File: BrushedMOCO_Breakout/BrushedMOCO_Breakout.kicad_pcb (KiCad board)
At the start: 2 copper layers, 24 parts, among them Q1 Si4156DY, Q2 Si4156DY, Q3 Si4156DY, Q4 Si4156DY, U1 74LVC2G04, U2 IRS2308, U3 IRS2308

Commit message: obscenely rough draft
sorry, this one may hurt to look at
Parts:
- added REF**: 4_40_Hole, MRDT_Drill_Holes:4_40_Hole, F.Cu at (131.1, 75.7)
- added REF**: 4_40_Hole, MRDT_Drill_Holes:4_40_Hole, F.Cu at (174.0, 75.7)
- added REF**: 4_40_Hole, MRDT_Drill_Holes:4_40_Hole, F.Cu at (174.0, 39.4)
- added REF**: 4_40_Hole, MRDT_Drill_Holes:4_40_Hole, F.Cu at (131.1, 39.4)
- moved Q4 27.4 mm to (157.6, 68.6), turned to -90 degrees
- moved Q3 24.0 mm to (164.2, 63.7), turned to 90 degrees
- moved R6 22.0 mm to (161.8, 39.9), turned to 90 degrees
- moved D1 21.4 mm to (145.0, 39.9), turned to 90 degrees
- moved Q1 20.4 mm to (140.6, 63.9), turned to -90 degrees
- moved U2 17.7 mm to (140.6, 41.8), turned to -90 degrees
- moved Q2 17.6 mm to (140.6, 50.5), turned to -90 degrees
- moved C2 16.0 mm to (146.3, 57.4), turned to 0 degrees
- moved D4 14.3 mm to (161.8, 44.1), turned to -90 degrees
- moved R1 13.1 mm to (145.0, 44.1)
- moved R5 13.1 mm to (160.0, 58.3)
- moved R2 13.1 mm to (138.7, 58.2)
- moved R3 11.4 mm to (136.4, 46.2), turned to -90 degrees
- moved C4 9.04 mm to (168.4, 49.9)
- moved D3 8.80 mm to (166.1, 47.8), turned to -90 degrees
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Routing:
- net +12V: track 0.00 -> 80.8 mm, vias 0 -> 5
- net /M-: track 0.00 -> 51.4 mm, vias 0 -> 2
- net (no net): track 0.00 -> 39.4 mm, vias 0 -> 2
- net /M+: track 0.00 -> 37.8 mm
- net Net-(D2-K): track 0.00 -> 32.0 mm, vias 0 -> 2
- net PWM_FWD: track 0.00 -> 23.9 mm, vias 0 -> 2
- net PWM_RVS: track 0.00 -> 18.8 mm, vias 0 -> 2
- net Net-(D1-A): track 0.00 -> 18.5 mm
- net Net-(D3-K): track 0.00 -> 15.8 mm
- net Net-(D4-A): track 0.00 -> 13.4 mm
- net Net-(Q4-G): track 0.00 -> 9.94 mm
- net +3V3: track 0.00 -> 9.52 mm
- net Net-(Q3-G): track 0.00 -> 7.27 mm
- net Net-(U2-LO): track 0.00 -> 2.70 mm
- net Net-(Q2-G): track 0.00 -> 2.64 mm
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- added copper zone on B.Cu, net GND
- added copper zone on F.Cu, net GND
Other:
- board outline added: 51.1 x 44.5 mm

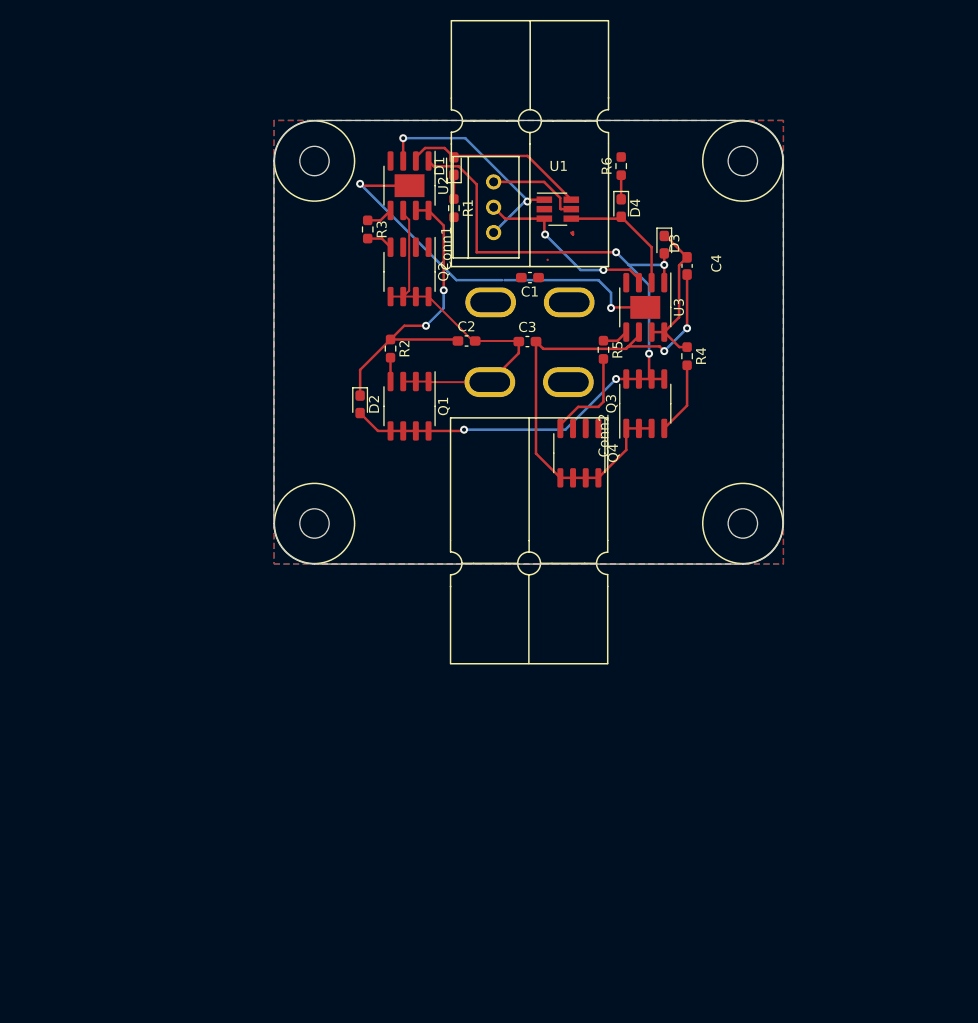
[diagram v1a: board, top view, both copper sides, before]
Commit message: A general outline of where stuff should go
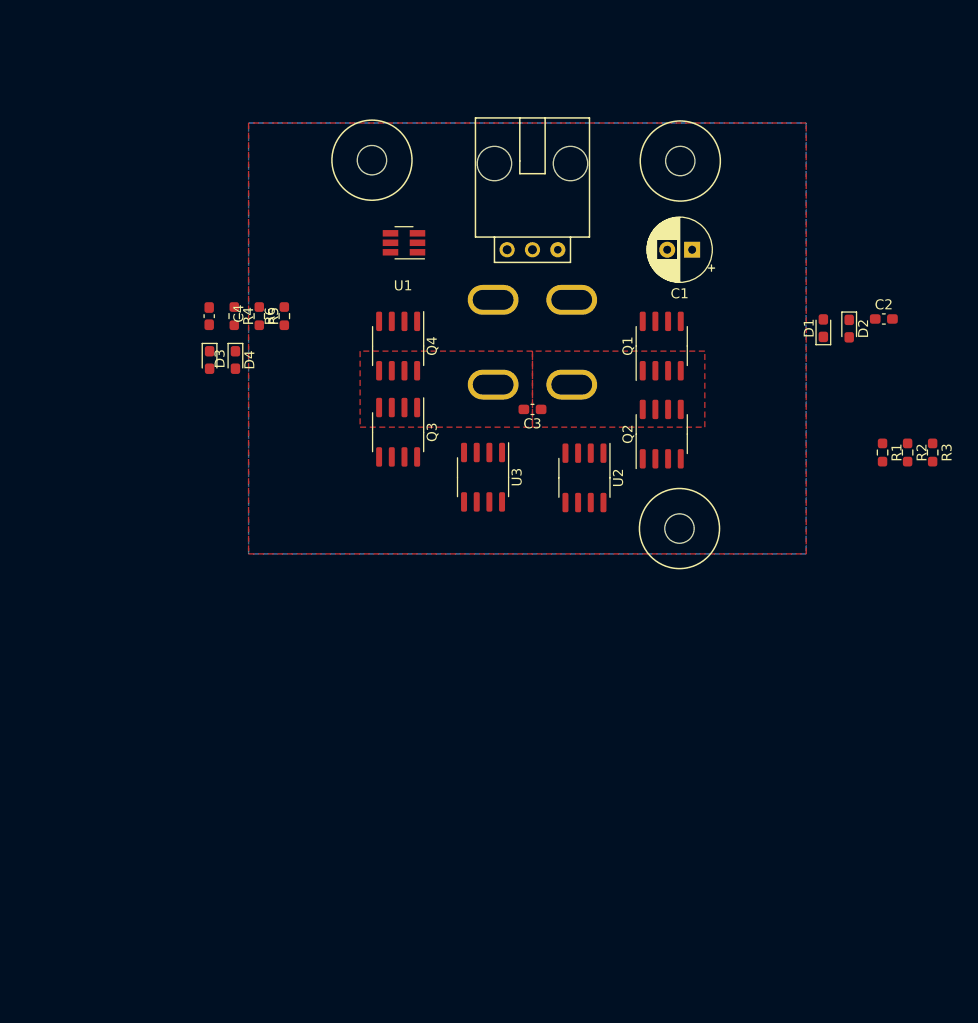
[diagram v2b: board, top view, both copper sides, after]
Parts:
- removed the REF** at (131.1, 75.7)
- removed the REF** at (174.0, 75.7)
- removed the REF** at (174.0, 39.4)
- removed the REF** at (131.1, 39.4)
- added REF**: 4_40_Hole, MRDT_Drill_Holes:4_40_Hole_Corner, F.Cu at (140.8, 43.3)
- added REF**: 4_40_Hole, MRDT_Drill_Holes:4_40_Hole_Corner, F.Cu at (163.7, 43.4)
- added REF**: 4_40_Hole, MRDT_Drill_Holes:4_40_Hole_Corner, F.Cu at (163.6, 72.2)
- C1: footprint Capacitor_SMD:C_0603_1608Metric_Pad1.08x0.95mm_HandSolder -> Capacitor_THT:CP_Radial_D6.3mm_P2.50mm
- Conn1, Conn2: footprint MRDT_Connectors:Square_Anderson_2_H_Side_By_Side_PV -> MRDT_Connectors:Square_Anderson_2_H_Side_By_Side; moved to B.Cu
- Conn3: footprint MRDT_Connectors:MOLEX_SL_03_Vertical -> MRDT_Connectors:MOLEX_SL_03_Horizontal
- U2, U3: footprint Package_SO:SOIC-8-1EP_3.9x4.9mm_P1.27mm_EP2.29x3mm -> Package_SO:SOIC-8_3.9x4.9mm_P1.27mm
- moved R3 60.9 mm to (193.0, 68.6)
- moved R2 52.9 mm to (190.5, 68.6)
- moved D2 49.6 mm to (184.6, 56.2)
- moved R1 49.4 mm to (188.0, 68.6)
- moved C4 48.2 mm to (120.5, 54.9)
- moved D3 47.0 mm to (120.6, 59.3)
- moved R4 45.6 mm to (123.0, 54.9)
- moved C2 41.9 mm to (188.1, 55.2)
- moved D4 41.5 mm to (123.1, 59.3)
- moved D1 40.4 mm to (182.1, 56.1)
- moved R6 37.0 mm to (128.0, 54.9)
- moved R5 34.7 mm to (125.5, 54.9)
- moved U2 34.1 mm to (158.1, 71.1)
- moved Q2 30.0 mm to (165.9, 66.7), turned to 90 degrees
- moved Q1 26.0 mm to (165.9, 57.9), turned to 90 degrees
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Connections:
- C1 pad 2: Net-(Conn1B-V+Log) -> +12V
- Conn3 pad 1: PWM_FWD -> PWM_RVS
- Conn3 pad 2: PWM_RVS -> PWM_FWD
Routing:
- net +12V: track 80.8 -> 0.00 mm, vias 5 -> 0
- net /M-: track 51.4 -> 0.00 mm, vias 2 -> 0
- net (no net): track 39.4 -> 0.00 mm, vias 2 -> 0
- net /M+: track 37.8 -> 0.00 mm
- net Net-(D2-K): track 32.0 -> 0.00 mm, vias 2 -> 0
- net PWM_FWD: track 23.9 -> 0.00 mm, vias 2 -> 0
- net PWM_RVS: track 18.8 -> 0.00 mm, vias 2 -> 0
- net Net-(D1-A): track 18.5 -> 0.00 mm
- net Net-(D3-K): track 15.8 -> 0.00 mm
- net Net-(D4-A): track 13.4 -> 0.00 mm
- net Net-(Q4-G): track 9.94 -> 0.00 mm
- net +3V3: track 9.52 -> 0.00 mm
- net Net-(Q3-G): track 7.27 -> 0.00 mm
- net Net-(U2-LO): track 2.70 -> 0.00 mm
- net Net-(Q2-G): track 2.64 -> 0.00 mm
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- added copper zone on B.Cu, net +12V
- added copper zone on F.Cu, net /M+
- added copper zone on F.Cu, net /M-
- removed copper zone on B.Cu, net GND
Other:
- board outline removed

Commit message: Some adjustments
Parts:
- removed the REF** at (140.8, 43.3)
- removed the REF** at (163.7, 43.4)
- removed the REF** at (163.6, 72.2)
- added REF**: 4_40_Hole, MRDT_Drill_Holes:4_40_Hole, F.Cu at (137.4, 80.3)
- added REF**: 4_40_Hole, MRDT_Drill_Holes:4_40_Hole, F.Cu at (105.7, 118.4)
- added REF**: 4_40_Hole, MRDT_Drill_Holes:4_40_Hole, F.Cu at (137.4, 118.4)
- added REF**: 4_40_Hole, MRDT_Drill_Holes:4_40_Hole, F.Cu at (105.7, 80.3)
- moved D1 83.3 mm to (126.2, 118.0)
- moved R1 81.2 mm to (123.5, 118.0), turned to 90 degrees
- moved R3 80.4 mm to (129.6, 118.1), turned to 0 degrees
- moved C2 68.1 mm to (138.9, 102.4), turned to 180 degrees
- moved D2 67.2 mm to (138.9, 105.4), turned to 0 degrees
- moved R2 65.2 mm to (138.9, 108.5), turned to 180 degrees
- moved R4 56.8 mm to (104.0, 108.5), turned to 0 degrees
- moved Q1 54.3 mm to (133.7, 101.7)
- moved Q2 54.2 mm to (133.7, 110.4)
- moved Q3 53.2 mm to (109.3, 110.4)
- moved Q4 53.1 mm to (109.3, 101.7)
- moved C3 52.9 mm to (121.5, 106.8)
- moved Conn2 52.8 mm to (126.0, 103.8)
- moved Conn3 51.7 mm to (119.0, 89.4)
- moved Conn1 51.7 mm to (117.1, 94.8)
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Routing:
- net Net-(D4-A): track 0.00 -> 36.3 mm
- net PWM_FWD: track 0.00 -> 36.3 mm
- net PWM_RVS: track 0.00 -> 34.3 mm, vias 0 -> 1
- net Net-(D2-K): track 0.00 -> 26.4 mm
- net +3V3: track 0.00 -> 21.6 mm, vias 0 -> 2
- net Net-(D3-K): track 0.00 -> 19.8 mm
- net Net-(U2-LO): track 0.00 -> 10.1 mm
- net Net-(U3-LO): track 0.00 -> 8.69 mm
- net Net-(Q4-G): track 0.00 -> 7.49 mm
- net Net-(Q2-G): track 0.00 -> 7.46 mm
- net Net-(Q1-G): track 0.00 -> 5.31 mm
- net Net-(D1-A): track 0.00 -> 5.01 mm
- net Net-(D1-K): track 0.00 -> 2.75 mm
- net Net-(Q3-G): track 0.00 -> 2.70 mm
- net Net-(D4-K): track 0.00 -> 2.31 mm

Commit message: save progress
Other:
- board outline added: 39.9 x 46.2 mm

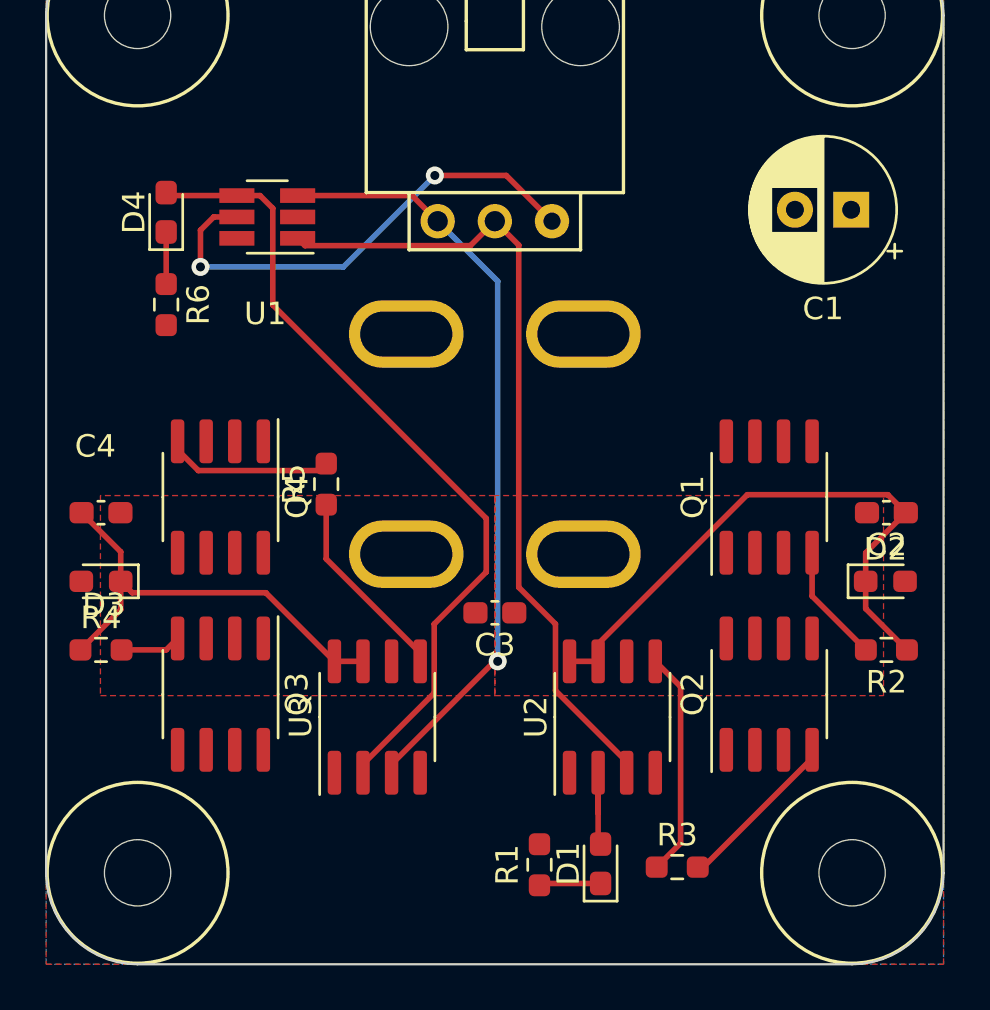
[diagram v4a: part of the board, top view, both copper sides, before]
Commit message: labels added
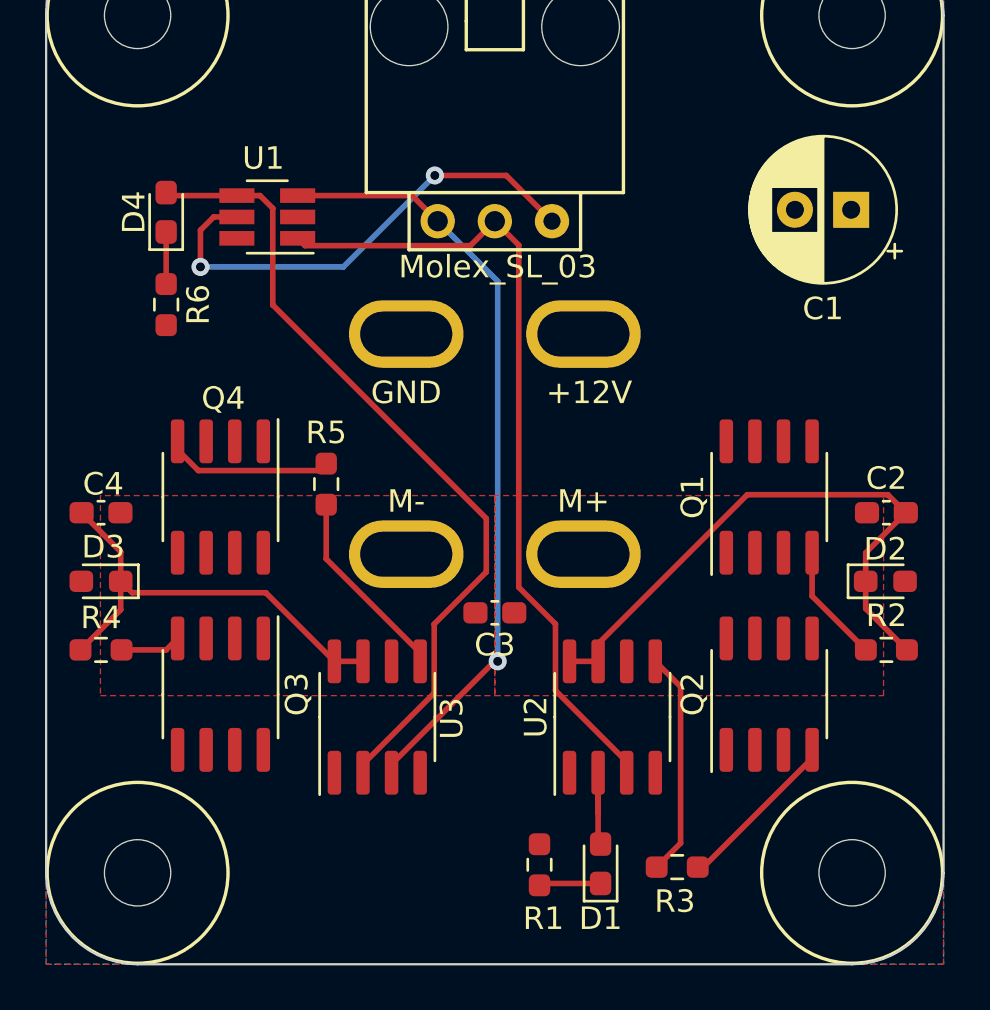
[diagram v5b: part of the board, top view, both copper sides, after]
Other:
- board text added: "+12V"
- board text added: "BrushedMOCO Breakout, Rev1 Mars Rover Design Team Missouri S&T, 2024 Nikolas Hidayat, Evan McGibney"
- board text added: "GND"
- board text added: "M+"
- board text added: "M-"
- board text added: "Molex_SL_03"
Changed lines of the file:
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@@
     (property "ki_keywords" "Gate Driver")
     (attr smd)
-    (fp_text reference "U3" (at 0 -3.4 90) (layer "F.SilkS")
+    (fp_text reference "U3" (at -0.065 3.319 90) (layer "F.SilkS")
         (effects (font (size 1 1) (thickness 0.15)))
     )
@@
     (property "ki_keywords" "R res resistor")
     (attr smd)
-    (fp_text reference "R5" (at 0 -1.43 90) (layer "F.SilkS")
+    (fp_text reference "R5" (at 2.286 0 180) (layer "F.SilkS")
         (effects (font (size 1 1) (thickness 0.15)))
     )
@@
     (property "ki_keywords" "Dual Gate NOT LVC CMOS")
     (attr smd)
-    (fp_text reference "U1" (at 0.092 -4.3) (layer "F.SilkS")
+    (fp_text reference "U1" (at 0.174 2.606) (layer "F.SilkS")
         (effects (font (size 1 1) (thickness 0.15)))
     )
@@
     (property "ki_keywords" "R res resistor")
     (attr smd)
-    (fp_text reference "R1" (at 0 -1.43 90) (layer "F.SilkS")
+    (fp_text reference "R1" (at -2.3895 0.175 180) (layer "F.SilkS")
         (effects (font (size 1 1) (thickness 0.15)))
     )
@@
     (property "ki_keywords" "R res resistor")
     (attr smd)
-    (fp_text reference "R2" (at 0 -1.43) (layer "F.SilkS")
+    (fp_text reference "R2" (at 0 1.524) (layer "F.SilkS")
         (effects (font (size 1 1) (thickness 0.15)))
     )
@@
     (property "ki_keywords" "LED diode")
     (attr smd)
-    (fp_text reference "D1" (at 0 -1.43 90) (layer "F.SilkS")
+    (fp_text reference "D1" (at -2.4345 0 180) (layer "F.SilkS")
         (effects (font (size 1 1) (thickness 0.15)))
     )
@@
     (property "ki_keywords" "diode")
     (attr smd)
-    (fp_text reference "D3" (at -0.127 -1.037) (layer "F.SilkS")
+    (fp_text reference "D3" (at -0.1005 1.524) (layer "F.SilkS")
         (effects (font (size 1 1) (thickness 0.15)))
     )
@@
     (property "ki_keywords" "R res resistor")
     (attr smd)
-    (fp_text reference "R3" (at 0 -1.43) (layer "F.SilkS")
+    (fp_text reference "R3" (at -0.1035 1.524) (layer "F.SilkS")
         (effects (font (size 1 1) (thickness 0.15)))
     )
@@
     (property "ki_keywords" "N-Channel MOSFET")
     (attr smd)
-    (fp_text reference "Q4" (at 0 -3.4 90) (layer "F.SilkS")
+    (fp_text reference "Q4" (at -4.383 -0.127 -180) (layer "F.SilkS")
         (effects (font (size 1 1) (thickness 0.15)))
     )
@@
     (property "ki_keywords" "cap capacitor")
     (attr smd)
-    (fp_text reference "C4" (at -0.254 -2.954) (layer "F.SilkS")
+    (fp_text reference "C4" (at 0.1005 -1.27) (layer "F.SilkS")
         (effects (font (size 1 1) (thickness 0.15)))
     )
@@
     (property "ki_keywords" "cap capacitor")
     (attr smd)
-    (fp_text reference "C2" (at 0 -1.43) (layer "F.SilkS")
+    (fp_text reference "C2" (at 0 1.524) (layer "F.SilkS")
         (effects (font (size 1 1) (thickness 0.15)))
     )
@@
     )
   )
+  (gr_line (start 121.539 90.8418) (end 121.539 107.7862)
+    (stroke (width 0.15) (type default)) (layer "B.SilkS"))
   (gr_arc (start 105.664 122.428) (mid 102.790318 121.237682) (end 101.6 118.364)
     (stroke (width 0.1) (type default)) (layer "Edge.Cuts"))
@@
   (gr_arc (start 101.6 80.264) (mid 102.790318 77.390318) (end 105.664 76.2)
     (stroke (width 0.1) (type default)) (layer "Edge.Cuts"))
+  (gr_text "BrushedMOCO Breakout, Rev1\nMars Rover Design Team \nMissouri S&T, 2024\nNikolas Hidayat, Evan McGibney " (at 134.140192 102.362) (layer "B.SilkS")
+    (effects (font (size 1 1) (thickness 0.15)) (justify left bottom mirror))
+  )
+  (gr_text "+12V" (at 125.73 97.028) (layer "F.SilkS")
+    (effects (font (size 1 1) (thickness 0.15)))
+  )
+  (gr_text "M+" (at 125.476 101.854) (layer "F.SilkS")
+    (effects (font (size 1 1) (thickness 0.15)))
+  )
+  (gr_text "Molex_SL_03" (at 121.666 91.44) (layer "F.SilkS")
+    (effects (font (size 1 1) (thickness 0.15)))
+  )
+  (gr_text "GND" (at 117.602 97.028) (layer "F.SilkS")
+    (effects (font (size 1 1) (thickness 0.15)))
+  )
+  (gr_text "M-" (at 117.602 101.854) (layer "F.SilkS")
+    (effects (font (size 1 1) (thickness 0.15)))
+  )
   (segment (start 139.8005 102.362) (end 139.0005 101.562) (width 0.25) (layer "F.Cu") (net 2))
   (segment (start 126.128 108.191249) (end 126.128 108.966) (width 0.25) (layer "F.Cu") (net 2))

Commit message: Signatures added
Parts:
- added G***: LOGO, LOGO, B.Cu at (133.9, 104.9)
- added G***: LOGO, LOGO, B.Cu at (108.5, 104.6)
